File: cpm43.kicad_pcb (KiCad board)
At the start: 2 copper layers, 231.3 x 76.8 mm, 185 parts, among them Q1 Q_NPN_BCE, SW1 SW_PUSH, U1 ATmega32U4, U2 PRTR5V0U2X, X1 Crystal_GND24

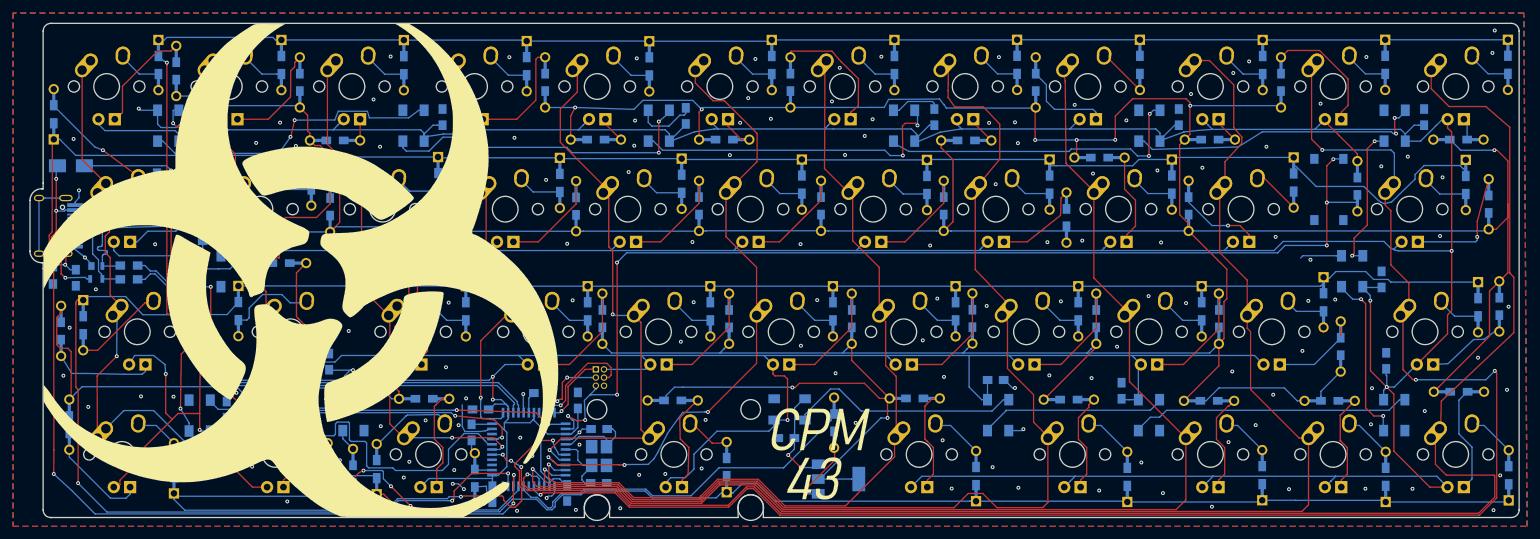
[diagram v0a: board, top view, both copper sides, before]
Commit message: Edge cuts have been changed
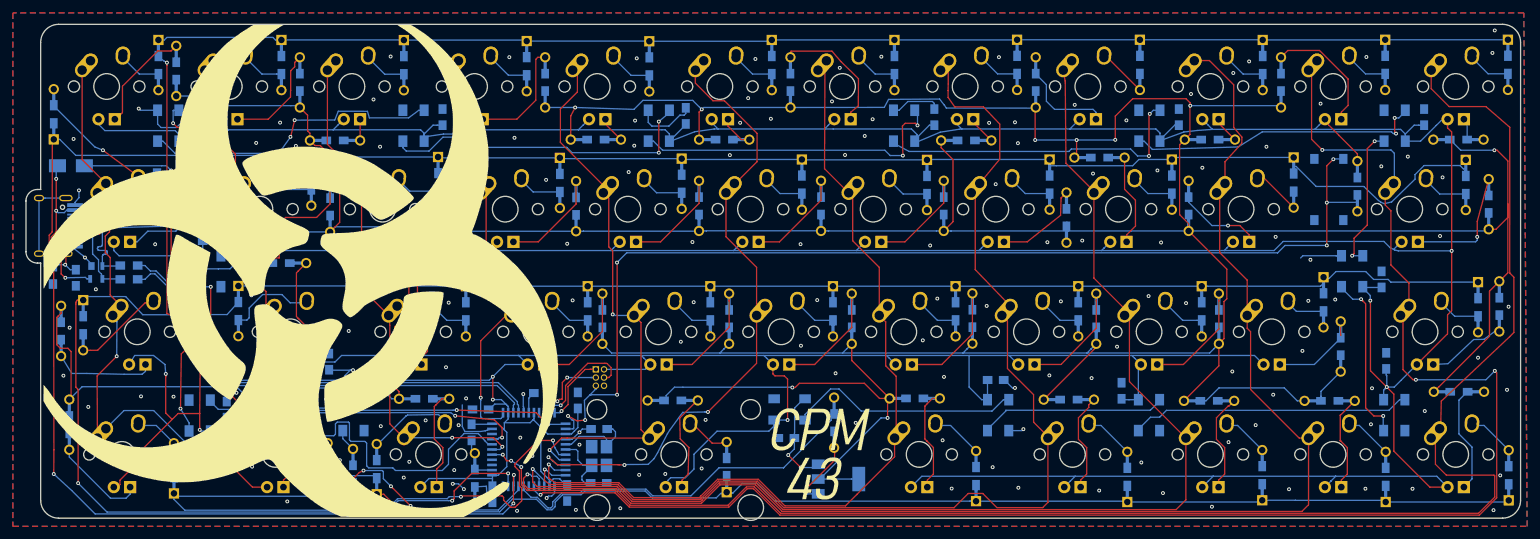
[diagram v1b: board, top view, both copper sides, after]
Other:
- board size 231.3 x 76.8 mm -> 232.2 x 76.7 mm
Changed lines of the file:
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@@
   (general
     (thickness 1.6)
-    (drawings 42)
-    (tracks 2369)
+    (drawings 27)
+    (tracks 2370)
     (zones 0)
     (modules 185)
@@
     (0 F.Cu signal)
     (31 B.Cu signal)
-    (32 B.Adhes user)
-    (33 F.Adhes user)
-    (34 B.Paste user)
-    (35 F.Paste user)
-    (36 B.SilkS user)
+    (32 B.Adhes user hide)
+    (33 F.Adhes user hide)
+    (34 B.Paste user hide)
+    (35 F.Paste user hide)
+    (36 B.SilkS user hide)
     (37 F.SilkS user)
-    (38 B.Mask user)
-    (39 F.Mask user)
+    (38 B.Mask user hide)
+    (39 F.Mask user hide)
     (40 Dwgs.User user hide)
-    (41 Cmts.User user)
-    (42 Eco1.User user)
-    (43 Eco2.User user)
+    (41 Cmts.User user hide)
+    (42 Eco1.User user hide)
+    (43 Eco2.User user hide)
     (44 Edge.Cuts user)
     (45 Margin user)
@@
     (trace_min 0.127)
     (segment_width 0.2)
-    (edge_width 0.1)
+    (edge_width 0.2)
     (via_size 0.6)
     (via_drill 0.3)
@@
       (usegerberadvancedattributes false)
       (creategerberjobfile false)
-      (excludeedgelayer true)
+      (excludeedgelayer false)
       (linewidth 0.100000)
       (plotframeref false)
@@
       (xy -7.940931 7.633607) (xy -6.563262 5.170714) (xy -6.247988 5.170714) (xy -6.14559 5.171216)) (layer F.SilkS) (width 0.01))
   )
-  (gr_line (start 33.42132 97.22612) (end 33.6557 97.22724) (layer Edge.Cuts) (width 0.1))
-  (gr_line (start 33.655 98.1329) (end 33.655 97.2256) (layer Edge.Cuts) (width 0.1))
-  (gr_line (start 34.8488 136.8044) (end 34.88944 136.8044) (layer Edge.Cuts) (width 0.1))
-  (gr_line (start 34.88944 136.8044) (end 34.85642 136.8044) (layer Edge.Cuts) (width 0.1))
-  (gr_line (start 117.729 136.8044) (end 34.8742 136.8044) (layer Edge.Cuts) (width 0.1))
-  (gr_line (start 145.5166 135.2296) (end 145.5166 136.8044) (layer Edge.Cuts) (width 0.1))
-  (gr_line (start 141.605161 135.254672) (end 141.605161 136.8044) (layer Edge.Cuts) (width 0.1))
-  (gr_line (start 121.6406 135.255) (end 121.6406 136.8044) (layer Edge.Cuts) (width 0.1))
-  (gr_line (start 117.729 135.2804) (end 117.729 136.8044) (layer Edge.Cuts) (width 0.1))
+  (gr_line (start 33.274 97.282) (end 32.766 97.282) (layer Edge.Cuts) (width 0.2))
+  (gr_line (start 32.766 85.852) (end 33.274 85.852) (layer Edge.Cuts) (width 0.2))
+  (gr_line (start 33.274 62.992) (end 33.274 85.852) (layer Edge.Cuts) (width 0.2))
+  (gr_line (start 33.274 97.282) (end 33.274 134.112) (layer Edge.Cuts) (width 0.2))
+  (gr_line (start 30.988 87.63) (end 30.988 95.504) (layer Edge.Cuts) (width 0.2))
+  (gr_arc (start 32.766 87.63) (end 32.766 85.852) (angle -90) (layer Edge.Cuts) (width 0.2))
+  (gr_arc (start 32.766 95.504) (end 30.988 95.504) (angle -90) (layer Edge.Cuts) (width 0.2))
+  (gr_line (start 36.068 60.198) (end 260.35 60.198) (layer Edge.Cuts) (width 0.2))
+  (gr_line (start 260.35 136.906) (end 36.068 136.906) (layer Edge.Cuts) (width 0.2))
+  (gr_line (start 263.144 62.992) (end 263.144 134.112) (layer Edge.Cuts) (width 0.2))
+  (gr_arc (start 260.35 62.992) (end 263.144 62.992) (angle -90) (layer Edge.Cuts) (width 0.2))
+  (gr_arc (start 260.35 134.112) (end 260.35 136.906) (angle -90) (layer Edge.Cuts) (width 0.2))
+  (gr_arc (start 36.068 134.112) (end 33.274 134.112) (angle -90) (layer Edge.Cuts) (width 0.2))
+  (gr_arc (start 36.068 62.992) (end 36.068 60.198) (angle -90) (layer Edge.Cuts) (width 0.2))
   (gr_text "Rev 1.0\n" (at 39.243 134.747) (layer B.SilkS)
     (effects (font (size 1.5 1.5) (thickness 0.3)) (justify mirror))
@@
   (gr_line (start 117.4242 128.6256) (end 116.9162 129.1336) (layer B.SilkS) (width 0.2))
   (gr_line (start 116.8908 128.0922) (end 117.4242 128.6256) (layer B.SilkS) (width 0.2))
-  (gr_line (start 141.605 136.8044) (end 121.6406 136.8044) (layer Edge.Cuts) (width 0.1))
-  (gr_line (start 145.5166 136.8044) (end 261.4676 136.8044) (layer Edge.Cuts) (width 0.1))
-  (gr_arc (start 119.684639 135.255328) (end 121.640439 135.255328) (angle -180.734521) (layer Edge.Cuts) (width 0.1))
-  (gr_arc (start 143.5608 135.2296) (end 145.5166 135.2296) (angle -180.734521) (layer Edge.Cuts) (width 0.1))
-  (gr_line (start 33.53308 85.74278) (end 33.4137 85.74024) (layer Edge.Cuts) (width 0.1))
-  (gr_line (start 33.53308 85.74278) (end 33.6423 85.74532) (layer Edge.Cuts) (width 0.1))
-  (gr_line (start 33.6423 85.74532) (end 33.655 85.73262) (layer Edge.Cuts) (width 0.1))
-  (gr_line (start 33.655 84.83854) (end 33.655 85.73262) (layer Edge.Cuts) (width 0.1))
-  (gr_line (start 31.61284 87.5411) (end 31.61284 95.4151) (layer Edge.Cuts) (width 0.1))
-  (gr_arc (start 33.426051 95.41256) (end 31.61284 95.41256) (angle -90) (layer Edge.Cuts) (width 0.1))
-  (gr_arc (start 33.426051 87.553451) (end 33.426051 85.74024) (angle -90) (layer Edge.Cuts) (width 0.1))
-  (gr_line (start 33.655 61.2648) (end 33.655 84.836) (layer Edge.Cuts) (width 0.1))
-  (gr_line (start 33.655 135.60806) (end 33.655 98.11766) (layer Edge.Cuts) (width 0.1))
-  (gr_line (start 261.4676 136.8044) (end 261.7216 136.8044) (layer Edge.Cuts) (width 0.1))
-  (gr_line (start 261.69874 60.0436) (end 34.87674 60.0436) (layer Edge.Cuts) (width 0.1))
-  (gr_line (start 262.91794 135.62838) (end 262.91794 61.25718) (layer Edge.Cuts) (width 0.1))
-  (gr_arc (start 261.6962 61.264374) (end 262.917514 61.264374) (angle -90) (layer Edge.Cuts) (width 0.1))
-  (gr_arc (start 261.69874 135.58266) (end 261.69874 136.803974) (angle -90) (layer Edge.Cuts) (width 0.1))
-  (gr_arc (start 34.876314 61.2648) (end 34.876314 60.043486) (angle -90) (layer Edge.Cuts) (width 0.1))
-  (gr_arc (start 34.850914 135.60806) (end 33.655 135.60806) (angle -90) (layer Edge.Cuts) (width 0.1))
   (gr_line (start 119.888 60.071) (end 183.642 56.769) (layer B.Fab) (width 0.2))
   (gr_line (start 115.824 70.358) (end 119.888 60.071) (layer B.Fab) (width 0.2))
@@
   (via (at 35.687 89.154) (size 0.6) (drill 0.3) (layers F.Cu B.Cu) (net 52))
   (segment (start 35.733101 89.200101) (end 35.687 89.154) (width 0.2032) (layer B.Cu) (net 52))
-  (segment (start 36.948069 89.200101) (end 35.733101 89.200101) (width 0.2032) (layer B.Cu) (net 52))
-  (segment (start 38.6115 89.0535) (end 37.09467 89.0535) (width 0.2032) (layer B.Cu) (net 52))
-  (segment (start 37.09467 89.0535) (end 36.948069 89.200101) (width 0.2032) (layer B.Cu) (net 52))
   (via (at 35.687 84.201) (size 0.6) (drill 0.3) (layers F.Cu B.Cu) (net 52))
   (segment (start 35.687 89.154) (end 35.687 84.201) (width 0.2032) (layer F.Cu) (net 52))
@@
   (segment (start 37.1094 99.568) (end 36.449 98.9838) (width 0.2032) (layer F.Cu) (net 52))
   (segment (start 36.449 98.9838) (end 36.449 96.9645) (width 0.2032) (layer F.Cu) (net 52))
+  (segment (start 35.986999 89.453999) (end 35.687 89.154) (width 0.2032) (layer B.Cu) (net 52))
+  (segment (start 36.938941 89.453999) (end 35.986999 89.453999) (width 0.2032) (layer B.Cu) (net 52))
+  (segment (start 37.33944 89.0535) (end 36.938941 89.453999) (width 0.2032) (layer B.Cu) (net 52))
+  (segment (start 38.6115 89.0535) (end 37.33944 89.0535) (width 0.2032) (layer B.Cu) (net 52))
   (segment (start 81.23428 119.85244) (end 66.1416 119.70512) (width 0.127) (layer B.Cu) (net 53))
   (segment (start 83.5015 118.504) (end 82.6745 118.504) (width 0.127) (layer B.Cu) (net 53))

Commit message: Hand soldering made not so hellish
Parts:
- moved R1 0.71 mm to (238.5, 85.3)
- moved XC1 0.38 mm to (120.0, 131.1)
- turned SW1 to 270 degrees
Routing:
- net VCC: track 30.2 -> 46.3 mm
- net Net-(C7-Pad2): track 21.7 -> 35.1 mm
- net GND: track 94.7 -> 102.0 mm, vias 161 -> 162
- net +5V: track 1198.2 -> 1201.5 mm
- net RST: track 169.8 -> 166.9 mm, vias 7 -> 6
- net COL5: track 98.2 -> 100.0 mm
- net ROW3: track 293.7 -> 292.3 mm
- net COL4: track 85.5 -> 86.7 mm
- net LEDPWM: track 58.5 -> 59.5 mm

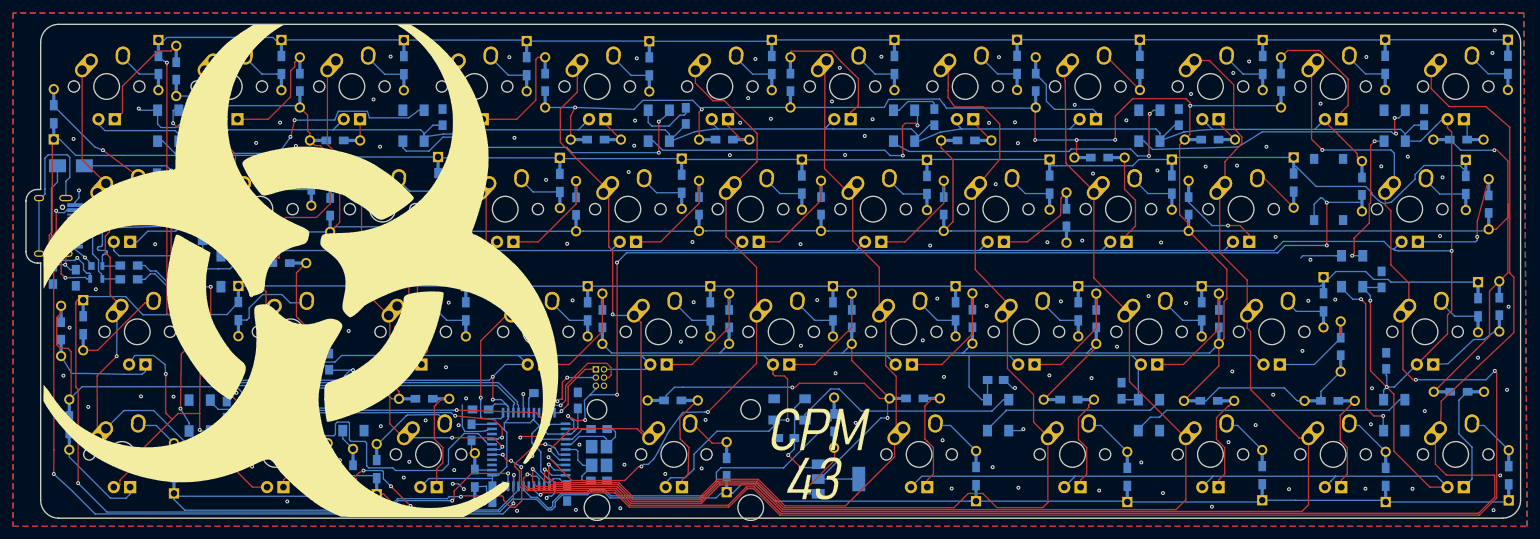
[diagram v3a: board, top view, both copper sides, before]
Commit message: Fixed stab holes
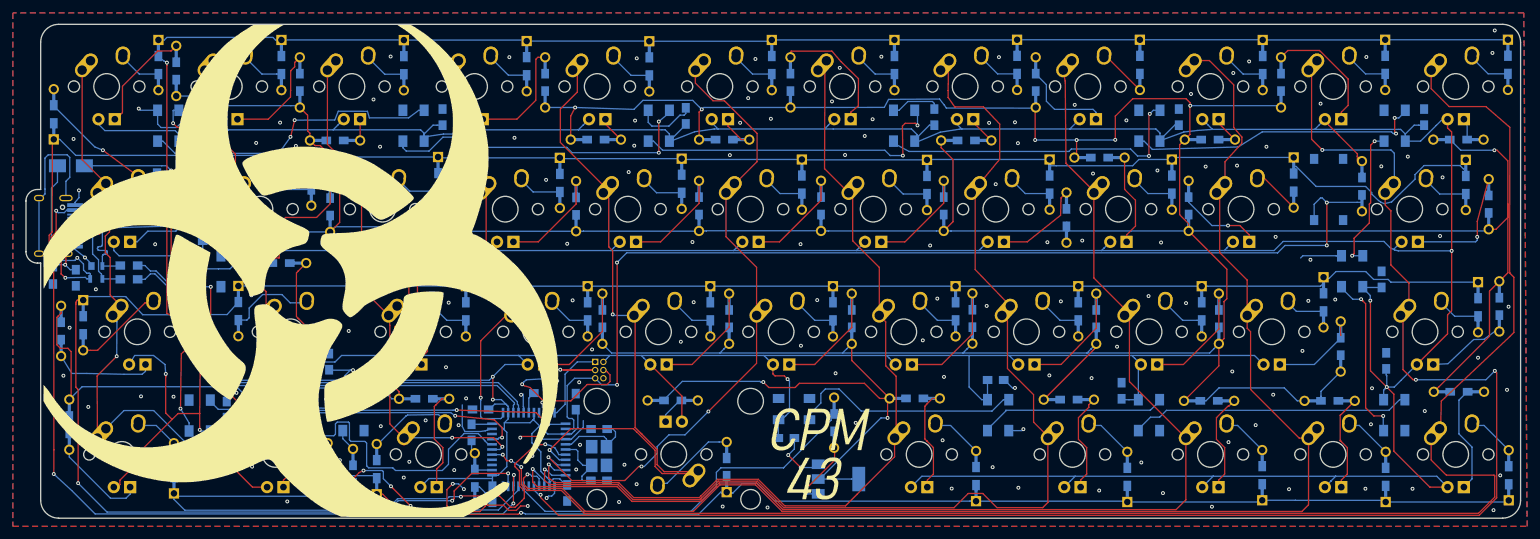
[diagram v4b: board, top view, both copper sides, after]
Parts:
- moved SPI1 1.17 mm to (119.4, 112.6)
- moved LED14 0.69 mm to (150.3, 120.0)
- moved C2 0.38 mm to (116.4, 118.8)
- turned MX38 to 180 degrees
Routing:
- net COL4: track 86.7 -> 111.6 mm
- net +5V: track 1201.5 -> 1183.6 mm
- net Net-(MX38-Pad4): track 15.6 -> 4.55 mm
- net GND: track 102.0 -> 113.1 mm, vias 162 -> 165
- net SCK: track 12.9 -> 23.4 mm, vias 2 -> 3
- net Net-(D38-Pad2): track 8.21 -> 14.5 mm
- net MOSI: track 17.7 -> 14.6 mm
- net ROW3: track 292.3 -> 289.4 mm
- net COL11: track 253.4 -> 251.1 mm
- net COL10: track 248.0 -> 245.7 mm
- net RST: track 166.9 -> 164.9 mm, vias 6 -> 4
- net COL9: track 215.3 -> 216.3 mm
- net LEDGND: track 836.4 -> 837.5 mm
- net Net-(R2-Pad1): track 6.42 -> 5.49 mm
- net LEDPWM: track 59.5 -> 58.9 mm
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
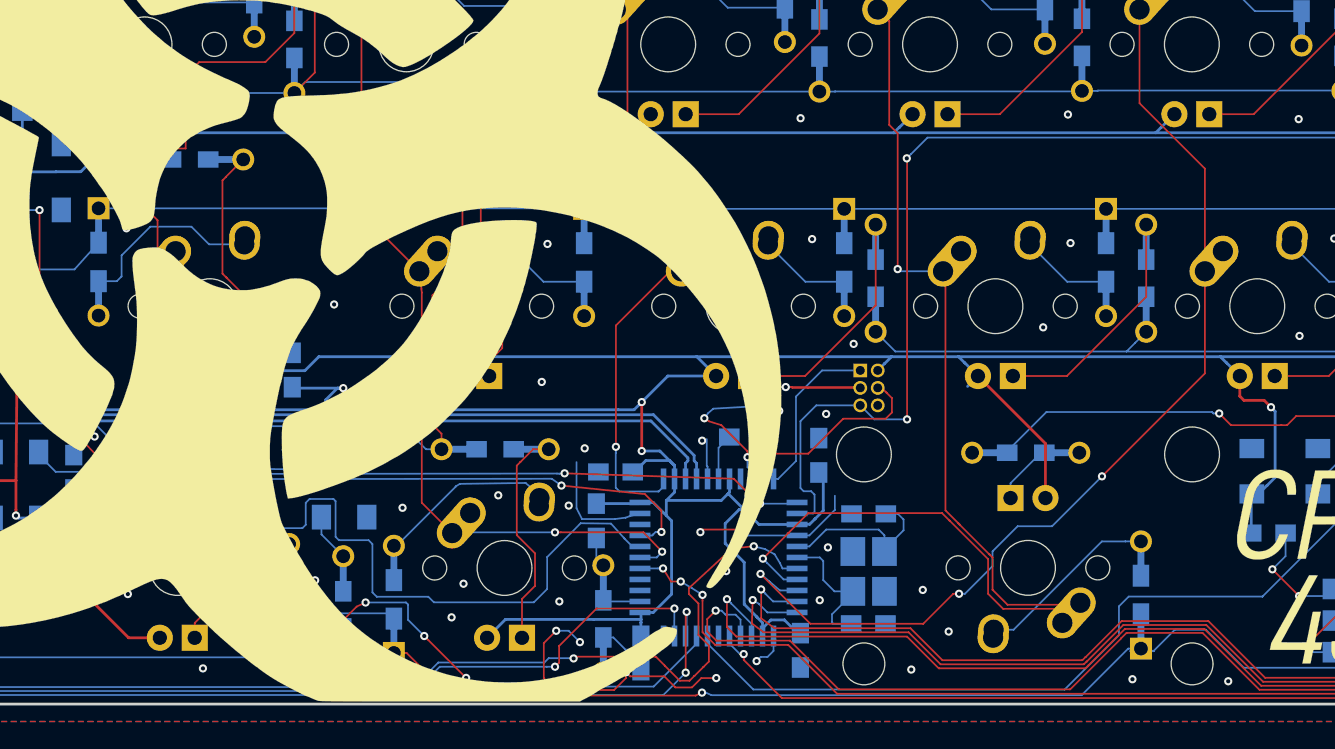
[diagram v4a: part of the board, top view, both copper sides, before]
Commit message: Bigger ICSP header
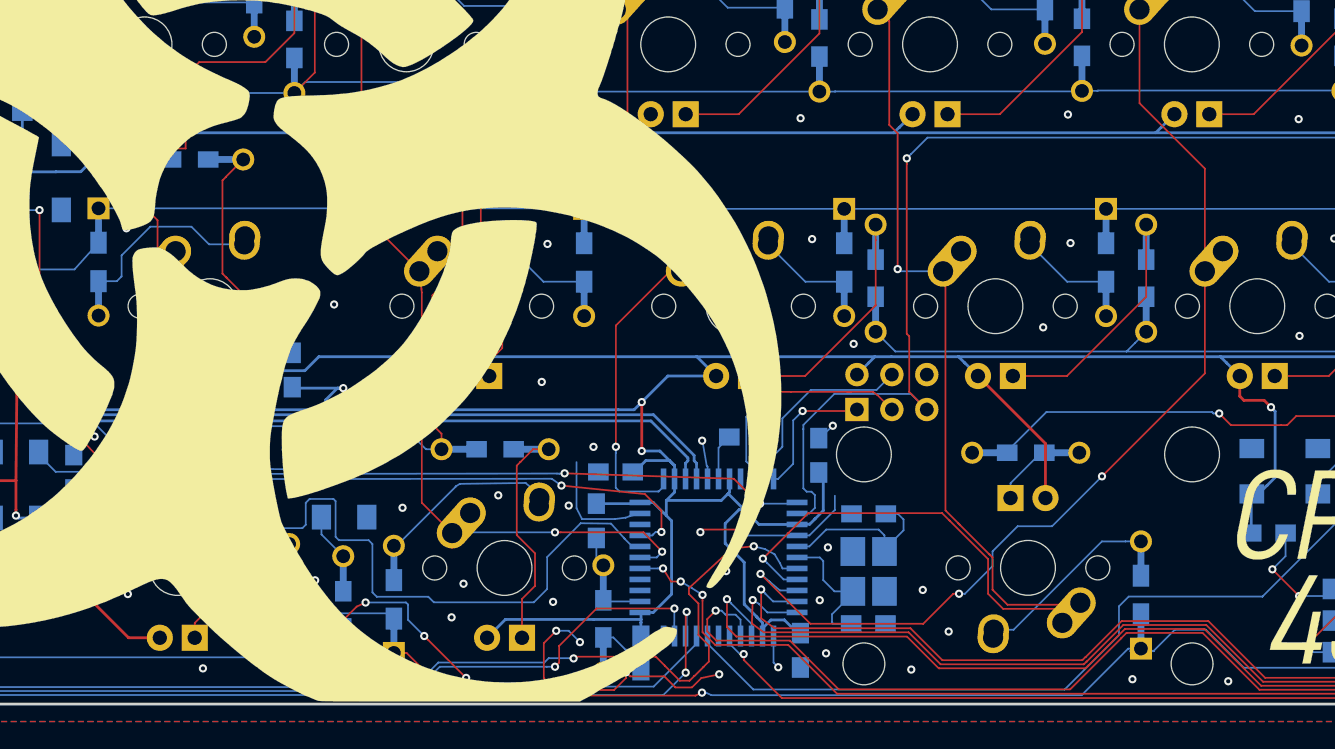
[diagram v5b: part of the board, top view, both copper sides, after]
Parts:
- SPI1: footprint keyboard_parts:Pin_Header_Straight_2x03_Pitch1.27mm -> keyboard_parts:Pin_Header_Straight_2x03_Pitch2.54mm
- moved SPI1 2.85 mm to (119.2, 115.5), turned to 90 degrees
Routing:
- net SCK: track 23.4 -> 16.8 mm, vias 3 -> 1
- net MISO: track 12.3 -> 10.0 mm, vias 0 -> 1
- net +5V: track 1183.6 -> 1182.1 mm
- net GND: track 113.1 -> 114.4 mm, vias 165 -> 167
- net RST: track 164.9 -> 166.0 mm, vias 4 -> 3
- net MOSI: track 14.6 -> 14.3 mm, vias 1 -> 0
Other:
- board text added: "0.1uF"
- board text added: "1.5K"
- board text added: "10K"
- board text added: "1uF"
- board text added: "22pF"
- board text added: "4.7uF"
- board text added: "Rev 2.0"
- board text removed: "Rev 1.0"

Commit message: New gerbers and Silkscreen changes
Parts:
- X1: value Crystal_GND24 -> (none); footprint Crystals:Crystal_SMD_3225-4pin_3.2x2.5mm_HandSoldering -> keyboard_parts:Crystal_SMD_3225-4pin_3.2x2.5mm
- moved SPI1 9.55 mm to (128.1, 118.8)
- moved R40 7.53 mm to (139.0, 118.1), turned to 90 degrees
- moved XC2 0.81 mm to (120.0, 123.9)
- moved XC1 0.64 mm to (120.0, 130.4)
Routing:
- net RST: track 166.0 -> 178.8 mm, vias 3 -> 5
- net MISO: track 10.0 -> 21.1 mm, vias 1 -> 2
- net MOSI: track 14.3 -> 24.8 mm
- net SCK: track 16.8 -> 27.1 mm, vias 1 -> 2
- net LEDGND: track 837.5 -> 827.3 mm
- net Net-(MX38-Pad4): track 4.55 -> 11.5 mm
- net +5V: track 1182.1 -> 1188.6 mm, vias 14 -> 15
- net Net-(U1-Pad16): track 12.6 -> 9.46 mm
- net Net-(U1-Pad17): track 10.2 -> 8.09 mm
